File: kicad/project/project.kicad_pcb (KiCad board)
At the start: 2 copper layers, 98 x 60 mm, 42 parts, among them J1 SWD, J3 Voltmeter, U1 ADS1015, U2 AP7380, U3 STM32L031F4Px, U4 VN7003ALH

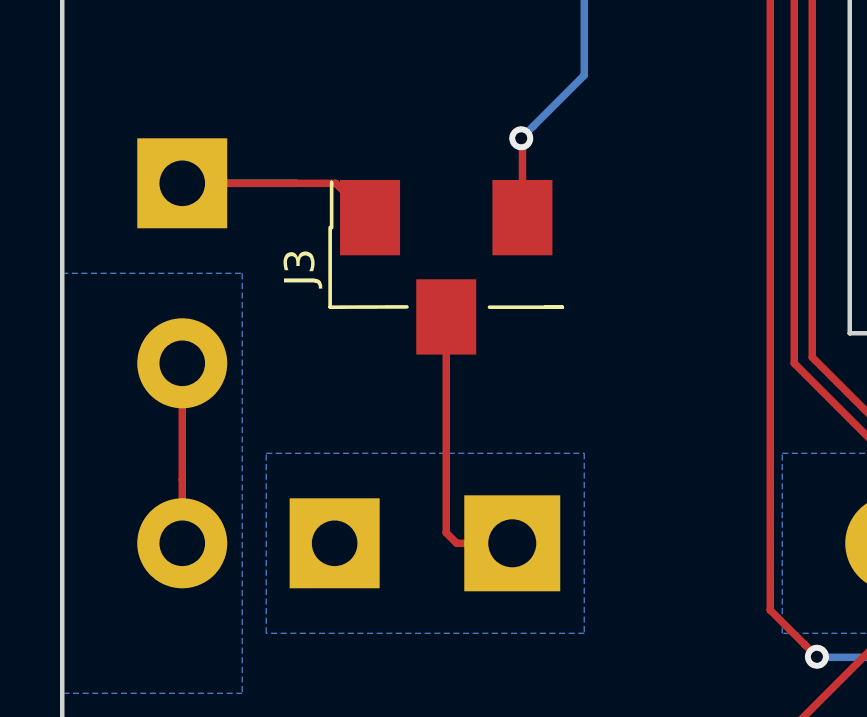
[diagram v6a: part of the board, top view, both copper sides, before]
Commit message: Voltmeter header
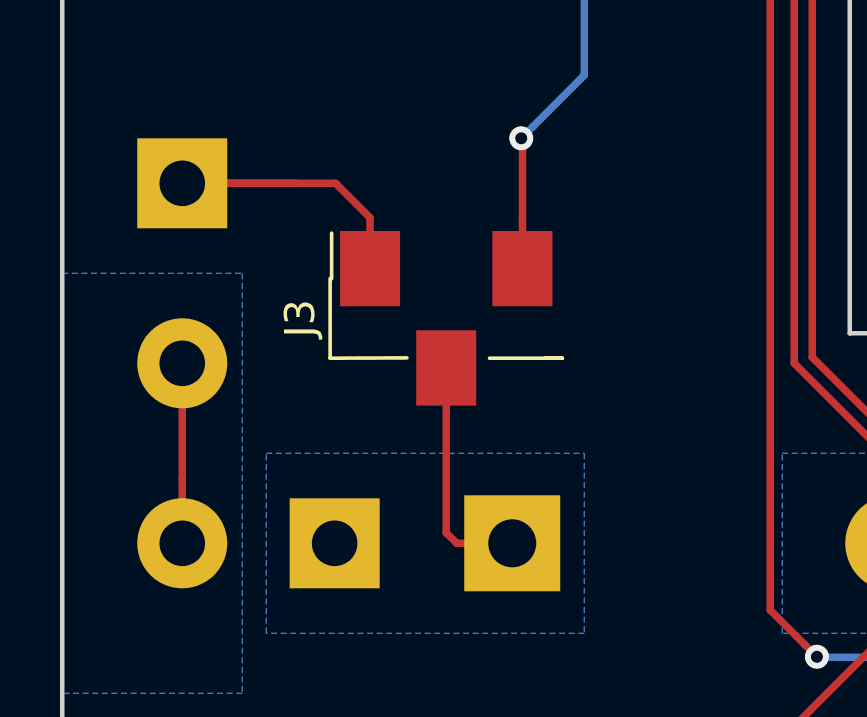
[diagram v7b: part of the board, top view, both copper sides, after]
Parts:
- J3: footprint theapi:Header_1x03_SMD_Pin1Right -> theapi:Voltmeter_Header_1x03
- moved J3 1.70 mm to (101.3, 100.5)
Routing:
- net /DIODE: track 9.54 -> 7.84 mm
- net GND: track 171.4 -> 173.1 mm
- net +24V: track 156.6 -> 158.3 mm
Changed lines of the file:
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@@
     (thickness 1.6)
     (drawings 25)
-    (tracks 475)
+    (tracks 477)
     (zones 0)
     (modules 42)
@@
     (add_net UART_TX)
   )
-  (module theapi:Header_1x03_SMD_Pin1Right (layer F.Cu)
-    (at 101.3 98.8 90)
+  (module theapi:Voltmeter_Header_1x03 (layer F.Cu)
+    (at 101.3 100.5 90)
     (descr "surface-mounted straight pin header, 1x03, 2.54mm pitch, single row, style 2 (pin 1 right)")
     (tags "Surface mounted pin header SMD 1x03 2.54mm single row style2 pin1 right")
@@
   (segment (start 183.5 109.92) (end 183.5 116.5) (width 0.25) (layer B.Cu) (net 1))
   (segment (start 181.58 108) (end 183.5 109.92) (width 0.25) (layer B.Cu) (net 1))
-  (segment (start 97.615 96) (end 98.76 97.145) (width 0.25) (layer F.Cu) (net 1))
   (segment (start 92.5 96) (end 97.615 96) (width 0.25) (layer F.Cu) (net 1))
   (segment (start 111.8 123.4) (end 111.95 123.4) (width 0.25) (layer F.Cu) (net 1))
@@
   (segment (start 110.889999 123.389999) (end 111.139999 123.389999) (width 0.25) (layer F.Cu) (net 1))
   (segment (start 110.8 122.4) (end 110.8 123.3) (width 0.25) (layer F.Cu) (net 1))
+  (segment (start 98.76 97.145) (end 98.76 98.845) (width 0.25) (layer F.Cu) (net 1))
+  (segment (start 97.615 96) (end 98.76 97.145) (width 0.25) (layer F.Cu) (net 1))
   (via (at 141.3 113.6) (size 0.8) (drill 0.4) (layers F.Cu B.Cu) (net 2))
   (via (at 141.3 111.2) (size 0.8) (drill 0.4) (layers F.Cu B.Cu) (net 2))
@@
   (segment (start 105.9 85.6) (end 105.9 92.4) (width 0.25) (layer B.Cu) (net 2))
   (segment (start 103.84 97.145) (end 103.84 94.54) (width 0.25) (layer F.Cu) (net 2))
+  (segment (start 103.84 97.145) (end 103.84 98.845) (width 0.25) (layer F.Cu) (net 2))
   (segment (start 170.6 125.825) (end 170.6 123.900002) (width 0.25) (layer F.Cu) (net 3))
   (segment (start 170.6 124.4) (end 170.6 123.900002) (width 0.25) (layer B.Cu) (net 3))
@@
   (segment (start 101.385 81.93) (end 101.375 81.92) (width 0.25) (layer B.Cu) (net 7))
   (segment (start 103.34 81.93) (end 101.385 81.93) (width 0.25) (layer B.Cu) (net 7))
-  (via (at 103.65 89) (size 0.8) (drill 0.4) (layers F.Cu B.Cu) (net 28))
-  (segment (start 103.55 88.9) (end 103.65 89) (width 0.25) (layer F.Cu) (net 28))
-  (segment (start 101.325 88.9) (end 103.55 88.9) (width 0.25) (layer F.Cu) (net 28))
-  (segment (start 101.45 89) (end 103.65 89) (width 0.25) (layer B.Cu) (net 28))
   (segment (start 160.099997 122.599999) (end 159.699998 122.2) (width 0.25) (layer B.Cu) (net 8))
   (segment (start 166.65 122.775) (end 160.274998 122.775) (width 0.25) (layer B.Cu) (net 8))
@@
   (segment (start 166.65 127.975) (end 140.901996 127.975) (width 0.25) (layer B.Cu) (net 27))
   (segment (start 140.901996 127.975) (end 138.6 125.673004) (width 0.25) (layer B.Cu) (net 27))
-  (segment (start 100.074072 88.400928) (end 99.575 88.9) (width 0.25) (layer F.Cu) (net 32))
-  (segment (start 104.675 83.8) (end 100.074072 88.400928) (width 0.25) (layer F.Cu) (net 32))
-  (segment (start 116.2 108) (end 116.2 105.3) (width 0.25) (layer F.Cu) (net 32))
-  (segment (start 110.3 83.8) (end 104.675 83.8) (width 0.25) (layer F.Cu) (net 32))
-  (segment (start 116.2 105.3) (end 112.9 102) (width 0.25) (layer F.Cu) (net 32))
-  (segment (start 112.9 102) (end 112.9 86.4) (width 0.25) (layer F.Cu) (net 32))
-  (segment (start 112.9 86.4) (end 110.3 83.8) (width 0.25) (layer F.Cu) (net 32))
+  (via (at 103.65 89) (size 0.8) (drill 0.4) (layers F.Cu B.Cu) (net 28))
+  (segment (start 103.55 88.9) (end 103.65 89) (width 0.25) (layer F.Cu) (net 28))
+  (segment (start 101.325 88.9) (end 103.55 88.9) (width 0.25) (layer F.Cu) (net 28))
+  (segment (start 101.45 89) (end 103.65 89) (width 0.25) (layer B.Cu) (net 28))
   (segment (start 178.600001 121.649999) (end 179 121.25) (width 0.25) (layer B.Cu) (net 29))
   (segment (start 170.50001 112.75001) (end 178.600001 120.850001) (width 0.25) (layer F.Cu) (net 29))
@@
   (segment (start 172.07499 131.32501) (end 166.065685 131.32501) (width 0.25) (layer B.Cu) (net 31))
   (segment (start 172.55 128.625) (end 172.55 130.85) (width 0.25) (layer B.Cu) (net 31))
+  (segment (start 100.074072 88.400928) (end 99.575 88.9) (width 0.25) (layer F.Cu) (net 32))
+  (segment (start 104.675 83.8) (end 100.074072 88.400928) (width 0.25) (layer F.Cu) (net 32))
+  (segment (start 116.2 108) (end 116.2 105.3) (width 0.25) (layer F.Cu) (net 32))
+  (segment (start 110.3 83.8) (end 104.675 83.8) (width 0.25) (layer F.Cu) (net 32))
+  (segment (start 116.2 105.3) (end 112.9 102) (width 0.25) (layer F.Cu) (net 32))
+  (segment (start 112.9 102) (end 112.9 86.4) (width 0.25) (layer F.Cu) (net 32))
+  (segment (start 112.9 86.4) (end 110.3 83.8) (width 0.25) (layer F.Cu) (net 32))
   (segment (start 100.624072 116.500928) (end 100.125 117) (width 0.25) (layer F.Cu) (net 32))
   (segment (start 116.2 108) (end 116.2 110.8) (width 0.25) (layer F.Cu) (net 32))
@@
   (segment (start 101.65 108) (end 103.5 108) (width 0.25) (layer F.Cu) (net 33))
   (segment (start 101.3 107.65) (end 101.65 108) (width 0.25) (layer F.Cu) (net 33))
-  (segment (start 101.3 100.455) (end 101.3 107.65) (width 0.25) (layer F.Cu) (net 33))
+  (segment (start 101.3 102.155) (end 101.3 107.65) (width 0.25) (layer F.Cu) (net 33))
   (zone (net 2) (net_name +24V) (layer B.Cu) (hatch edge 0.508)
     (priority 10)

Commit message: Solder mask
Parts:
- moved R11 0.30 mm to (137.5, 127.9)
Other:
- rule pad_to_mask_clearance: 0.051 -> 0
